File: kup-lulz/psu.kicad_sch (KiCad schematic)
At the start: 117 parts, among them J1 CONN_PCIE_PWR_8PIN, J2 CONN_IBC_MGMT, J3 CONN_01X03, J4 CONN_01X05, Q1 SSM6N58NU, SW1 SWITCH, SW2 SWITCH, U1 STM32L031C6U6, U2 MYMGK1R812ERSR, U3 MYMGK1R812ERSR, U4 MYMGK00506ERSR, U5 MYMGK00504ERSR, U6 MYMGK00504ERSR, U7 MYMGK00504ERSR, U8 ADP1740ACPZ-1.8-R7

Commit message: Continued initial work on kup-lulz devboard
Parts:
- C40, C41: footprint (none) -> azonenberg_pcb:EIA_0603_CAP_NOSILK
- Q1: footprint (none) -> azonenberg_pcb:DFN_6_0.65MM_2x2MM_GDS
- R31: footprint (none) -> azonenberg_pcb:EIA_0402_RES_NOSILK
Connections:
- net 1V8: no longer U4.5 (SENSE)
- net 3V3: now also U4.5 (SENSE)
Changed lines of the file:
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@@
   (title_block
     (title "Kintex Ultrascale+ OshPark For The Lulz")
-    (date "2024-01-31")
+    (date "2024-02-01")
     (rev "0.1")
   )
@@
     (effects (font (size 1.27 1.27)) (justify left bottom))
   )
-  (label "1V8" (at 245.11 109.22 0)
+  (label "3V3" (at 245.11 109.22 0)
     (effects (font (size 1.27 1.27)) (justify left bottom))
   )
@@
     (effects (font (size 1.27 1.27)) (justify right))
   )
-  (hierarchical_label "FPGA_INIT" (shape bidirectional) (at 91.44 393.7 180)
+  (hierarchical_label "FPGA_INIT" (shape input) (at 91.44 393.7 180)
     (effects (font (size 1.27 1.27)) (justify right))
   )
@@
       (effects (font (size 1.27 1.27)) (justify left))
     )
-    (property "Footprint" "" (id 2) (at 357.8352 154.94 0)
+    (property "Footprint" "azonenberg_pcb:EIA_0603_CAP_NOSILK" (id 2) (at 357.8352 154.94 0)
       (effects (font (size 1.27 1.27)) hide)
     )
@@
       (effects (font (size 1.524 1.524)) (justify left))
     )
-    (property "Footprint" "" (id 2) (at 382.27 204.47 0)
+    (property "Footprint" "azonenberg_pcb:DFN_6_0.65MM_2x2MM_GDS" (id 2) (at 382.27 204.47 0)
       (effects (font (size 1.524 1.524)) hide)
     )
@@
       (effects (font (size 1.27 1.27)) (justify left))
     )
-    (property "Footprint" "" (id 2) (at 406.0952 154.94 0)
+    (property "Footprint" "azonenberg_pcb:EIA_0603_CAP_NOSILK" (id 2) (at 406.0952 154.94 0)
       (effects (font (size 1.27 1.27)) hide)
     )
@@
       (effects (font (size 1.27 1.27)) (justify left))
     )
-    (property "Footprint" "" (id 2) (at 383.032 193.04 90)
+    (property "Footprint" "azonenberg_pcb:EIA_0402_RES_NOSILK" (id 2) (at 383.032 193.04 90)
       (effects (font (size 1.27 1.27)) hide)
     )

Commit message: Continued initial layout of kup-lulz
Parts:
- C39: footprint (none) -> azonenberg_pcb:EIA_0402_CAP_NOSILK
- U8: footprint (none) -> azonenberg_pcb:QFN_16_0.65MM_4x4MM
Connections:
- net GND: now also U8.6 (GND), U8.PAD (GND)
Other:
- company: (none) -> Antikernel Labs
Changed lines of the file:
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@@
   (title_block
     (title "Kintex Ultrascale+ OshPark For The Lulz")
-    (date "2024-02-01")
+    (date "2024-02-05")
     (rev "0.1")
+    (company "Antikernel Labs")
+    (comment 1 "Andrew D. Zonenberg")
   )
   (junction (at 222.25 139.7) (diameter 0) (color 0 0 0 0)
@@
     (effects (font (size 1.27 1.27)) (justify right bottom))
   )
+  (label "GND" (at 369.57 170.18 180)
+    (effects (font (size 1.27 1.27)) (justify right bottom))
+  )
   (label "BOOT0" (at 195.58 401.32 180)
     (effects (font (size 1.27 1.27)) (justify right bottom))
@@
     (property "Reference" "U8" (id 0) (at 384.175 142.4772 0))
     (property "Value" "ADP1740ACPZ-1.8-R7" (id 1) (at 384.175 145.0141 0))
-    (property "Footprint" "" (id 2) (at 374.65 175.26 0)
+    (property "Footprint" "azonenberg_pcb:QFN_16_0.65MM_4x4MM" (id 2) (at 374.65 175.26 0)
       (effects (font (size 1.27 1.27)) hide)
     )
@@
       (effects (font (size 1.27 1.27)) (justify left))
     )
-    (property "Footprint" "" (id 2) (at 348.9452 170.18 0)
+    (property "Footprint" "azonenberg_pcb:EIA_0402_CAP_NOSILK" (id 2) (at 348.9452 170.18 0)
       (effects (font (size 1.27 1.27)) hide)
     )

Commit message: Continued initial layout
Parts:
- removed C14, C18: 22 uF 25V, azonenberg_pcb:EIA_1812_CAP_NOSILK, symbol device:C
- removed C28, C32: 220 uF, azonenberg_pcb:EIA_1210_CAP_NOSILK, symbol device:C
- removed C36: DNP, azonenberg_pcb:EIA_1210_CAP_NOSILK, symbol device:C
- removed R18: 3k, azonenberg_pcb:EIA_0402_RES_NOSILK, symbol device:R
- removed R22: 160, azonenberg_pcb:EIA_0402_RES_NOSILK, symbol device:R
- removed R36: 10K, azonenberg_pcb:EIA_0402_RES_NOSILK, symbol device:R
- removed R37: 1K, azonenberg_pcb:EIA_0402_RES_NOSILK, symbol device:R
- removed TP17: U.FL, azonenberg_pcb:CONN_U.FL_TE_1909763-1, symbol conn:CONN_COAXIAL
- removed TP5: TESTPOINT, azonenberg_pcb:TESTPOINT_SMT_0.5MM, symbol conn:CONN_01X01
- removed U6: MYMGK00504ERSR, azonenberg_pcb:MODULE_MURATA_MYMGK00504ERSR, symbol power-azonenberg:MYMGK00504ERSR
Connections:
- net 2V5 is gone; now on net 3V3: C40.1, R31.1, U8.1 (VIN), U8.15 (VIN), U8.16 (VIN), U8.2 (VIN), U8.3 (VIN)
- net 2V5_EN: no longer names the net of U1.1 (PC0)
- net 2V5_PGOOD: no longer names the net of U1.2 (PC13)
- net GVEN_2V5 renamed GVEN_3V3
- no-connect marks 4 -> 6
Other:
- note added: "220 mA @ 1.8V regulated from some other rail Use 3V3 for input on test board to eliminate need for 2V5 rail on an already dense PCB"
- note added: "Level shift GTY_VCCAUX_EN to 3.3V levels since EN of ADP1740 should not exceed VIN"
- note removed: "220 mA @ 1.8V regulated from some other rail 2V5 has plenty of headroom if regulator has <700 mV dropout"
- note removed: "Level shift GTY_VCCAUX_EN to 2.5V levels since EN of ADP1740 should not exceed VIN"
- moved on the sheet: TP16

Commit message: Continued initial routing
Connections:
- net 1V8_EN: now also U1.4 (PC15); no longer U1.27 (PB14)
- net 1V8_PGOOD: now also U1.3 (PC14); no longer U1.28 (PB15)
- net 3V3_EN: now also U1.10 (PA0); no longer U1.20 (PB2)
- net 3V3_PGOOD: now also U1.11 (PA1); no longer U1.18 (PB0)
- net FPGA_RST_N: now also U1.18 (PB0); no longer U1.11 (PA1)
- net GTY_VCCAUX_EN_N: now also U1.28 (PB15); no longer U1.3 (PC14)
- net GTY_VCCAUX_PGOOD: now also U1.27 (PB14); no longer U1.4 (PC15)
- net GTY_VCC_EN: now also U1.12 (PA2); no longer U1.21 (PB10)
- net GTY_VTT_EN: now also U1.30 (PA9); no longer U1.41 (PB5)
- net MCU_READY: now also U1.20 (PB2); no longer U1.10 (PA0)
- net MCU_RST_N: now also U1.21 (PB10); no longer U1.12 (PA2)
- net SUPER_I2C_SCL: now also U1.45 (PB8); no longer U1.30 (PA9)
- net SUPER_I2C_SDA: now also U1.46 (PB9); no longer U1.31 (PA10)
- net VCCINT_EN: now also U1.2 (PC13); no longer U1.39 (PB3)
- net VCCINT_PGOOD: now also U1.1 (PC0); no longer U1.32 (PA11)
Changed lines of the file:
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@@
   )
   (no_connect (at 48.26 370.84))
-  (no_connect (at 130.81 396.24))
-  (no_connect (at 91.44 383.54))
-  (no_connect (at 91.44 386.08))
+  (no_connect (at 91.44 375.92))
+  (no_connect (at 48.26 391.16))
+  (no_connect (at 91.44 370.84))
   (no_connect (at 91.44 373.38))
-  (no_connect (at 130.81 393.7))
+  (no_connect (at 48.26 388.62))
   (wire (pts (xy 67.31 214.63) (xy 67.31 217.17))
     (stroke (width 0) (type default) (color 0 0 0 0))
@@
     (effects (font (size 1.27 1.27)) (justify right bottom))
   )
-  (label "1V8_PGOOD" (at 91.44 401.32 180)
+  (label "1V8_PGOOD" (at 130.81 398.78 180)
     (effects (font (size 1.27 1.27)) (justify right bottom))
   )
@@
     (effects (font (size 1.27 1.27)) (justify right bottom))
   )
-  (label "3V3_EN" (at 91.44 368.3 180)
+  (label "3V3_EN" (at 48.26 363.22 180)
     (effects (font (size 1.27 1.27)) (justify right bottom))
   )
@@
     (effects (font (size 1.27 1.27)) (justify left bottom))
   )
-  (label "SUPER_I2C_SDA" (at 48.26 388.62 180)
+  (label "SUPER_I2C_SDA" (at 91.44 386.08 180)
     (effects (font (size 1.27 1.27)) (justify right bottom))
   )
@@
     (effects (font (size 1.27 1.27)) (justify left bottom))
   )
-  (label "VCCINT_PGOOD" (at 48.26 391.16 180)
+  (label "VCCINT_PGOOD" (at 130.81 393.7 180)
     (effects (font (size 1.27 1.27)) (justify right bottom))
   )
@@
     (effects (font (size 1.27 1.27)) (justify right bottom))
   )
-  (label "GTY_VCCAUX_PGOOD" (at 130.81 401.32 180)
+  (label "GTY_VCCAUX_PGOOD" (at 91.44 398.78 180)
     (effects (font (size 1.27 1.27)) (justify right bottom))
   )
@@
     (effects (font (size 1.27 1.27)) (justify right bottom))
   )
-  (label "VCCINT_EN" (at 91.44 370.84 180)
+  (label "VCCINT_EN" (at 130.81 396.24 180)
     (effects (font (size 1.27 1.27)) (justify right bottom))
   )
@@
     (effects (font (size 1.27 1.27)) (justify right bottom))
   )
-  (label "1V8_EN" (at 91.44 398.78 180)
+  (label "1V8_EN" (at 130.81 401.32 180)
     (effects (font (size 1.27 1.27)) (justify right bottom))
   )
-  (label "GTY_VTT_EN" (at 91.44 375.92 180)
+  (label "GTY_VTT_EN" (at 48.26 386.08 180)
     (effects (font (size 1.27 1.27)) (justify right bottom))
   )
@@
     (effects (font (size 1.27 1.27)) (justify right bottom))
   )
-  (label "SUPER_I2C_SCL" (at 48.26 386.08 180)
+  (label "SUPER_I2C_SCL" (at 91.44 383.54 180)
     (effects (font (size 1.27 1.27)) (justify right bottom))
   )
@@
     (effects (font (size 1.27 1.27)) (justify left bottom))
   )
-  (label "3V3_PGOOD" (at 91.44 363.22 180)
+  (label "3V3_PGOOD" (at 48.26 365.76 180)
     (effects (font (size 1.27 1.27)) (justify right bottom))
   )
@@
     (effects (font (size 1.27 1.27)) (justify right bottom))
   )
-  (label "GTY_VCCAUX_EN_N" (at 130.81 398.78 180)
+  (label "GTY_VCCAUX_EN_N" (at 91.44 401.32 180)
     (effects (font (size 1.27 1.27)) (justify right bottom))
   )
@@
     (effects (font (size 1.27 1.27)) (justify right bottom))
   )
-  (label "GTY_VCC_EN" (at 91.44 388.62 180)
+  (label "GTY_VCC_EN" (at 48.26 368.3 180)
     (effects (font (size 1.27 1.27)) (justify right bottom))
   )
@@
     (effects (font (size 1.27 1.27)) (justify right))
   )
-  (hierarchical_label "MCU_READY" (shape input) (at 48.26 363.22 180)
+  (hierarchical_label "MCU_READY" (shape input) (at 91.44 368.3 180)
     (effects (font (size 1.27 1.27)) (justify right))
   )
@@
     (effects (font (size 1.27 1.27)) (justify left))
   )
-  (hierarchical_label "MCU_RST_N" (shape output) (at 48.26 368.3 180)
+  (hierarchical_label "MCU_RST_N" (shape output) (at 91.44 388.62 180)
     (effects (font (size 1.27 1.27)) (justify right))
   )
@@
     (effects (font (size 1.27 1.27)) (justify right))
   )
-  (hierarchical_label "FPGA_RST_N" (shape output) (at 48.26 365.76 180)
+  (hierarchical_label "FPGA_RST_N" (shape output) (at 91.44 363.22 180)
     (effects (font (size 1.27 1.27)) (justify right))
   )
@@
     (pin "17")
     (pin "29")
-    (pin "30" (alternate "I2C1_SCL"))
-    (pin "31" (alternate "I2C1_SDA"))
+    (pin "30")
+    (pin "31")
     (pin "32")
     (pin "33")
@@
     (pin "40")
     (pin "41")
-    (pin "42")
-    (pin "43")
-    (pin "45")
-    (pin "46")
+    (pin "42" (alternate "USART2_TX"))
+    (pin "43" (alternate "USART2_RX"))
+    (pin "45" (alternate "I2C1_SCL"))
+    (pin "46" (alternate "I2C1_SDA"))
     (pin "1")
     (pin "2")
@@
     (pin "17")
     (pin "29")
-    (pin "30" (alternate "I2C1_SCL"))
-    (pin "31" (alternate "I2C1_SDA"))
+    (pin "30")
+    (pin "31")
     (pin "32")
     (pin "33")
@@
     (pin "40")
     (pin "41")
-    (pin "42")
-    (pin "43")
-    (pin "45")
-    (pin "46")
+    (pin "42" (alternate "USART2_TX"))
+    (pin "43" (alternate "USART2_RX"))
+    (pin "45" (alternate "I2C1_SCL"))
+    (pin "46" (alternate "I2C1_SDA"))
     (pin "1")
     (pin "2")
@@
     (pin "15" (alternate "SPI1_SCK"))
     (pin "16" (alternate "SPI1_MISO"))
-    (pin "17" (alternate "SPI1_MOSI"))
+    (pin "17")
     (pin "29")
-    (pin "30" (alternate "I2C1_SCL"))
-    (pin "31" (alternate "I2C1_SDA"))
+    (pin "30")
+    (pin "31")
     (pin "32")
     (pin "33")
-    (pin "34" (alternate "SWDIO"))
-    (pin "37" (alternate "SWCLK"))
+    (pin "34")
+    (pin "37")
     (pin "38")
     (pin "18")
@@
     (pin "40")
     (pin "41")
-    (pin "42")
-    (pin "43")
-    (pin "45")
-    (pin "46")
+    (pin "42" (alternate "USART2_TX"))
+    (pin "43" (alternate "USART2_RX"))
+    (pin "45" (alternate "I2C1_SCL"))
+    (pin "46" (alternate "I2C1_SDA"))
     (pin "1")
     (pin "2")
@@
     (pin "17")
     (pin "29")
-    (pin "30" (alternate "I2C1_SCL"))
-    (pin "31" (alternate "I2C1_SDA"))
+    (pin "30")
+    (pin "31")
     (pin "32")
     (pin "33")
@@
     (pin "40")
     (pin "41")
-    (pin "42")
-    (pin "43")
-    (pin "45")
-    (pin "46")
+    (pin "42" (alternate "USART2_TX"))
+    (pin "43" (alternate "USART2_RX"))
+    (pin "45" (alternate "I2C1_SCL"))
+    (pin "46" (alternate "I2C1_SDA"))
     (pin "1")
     (pin "2")
@@
     (pin "17")
     (pin "29")
-    (pin "30" (alternate "I2C1_SCL"))
-    (pin "31" (alternate "I2C1_SDA"))
+    (pin "30")
+    (pin "31")
     (pin "32")
     (pin "33")
@@
     (pin "42" (alternate "USART2_TX"))
     (pin "43" (alternate "USART2_RX"))
-    (pin "45")
-    (pin "46")
+    (pin "45" (alternate "I2C1_SCL"))
+    (pin "46" (alternate "I2C1_SDA"))
     (pin "1")
     (pin "2")

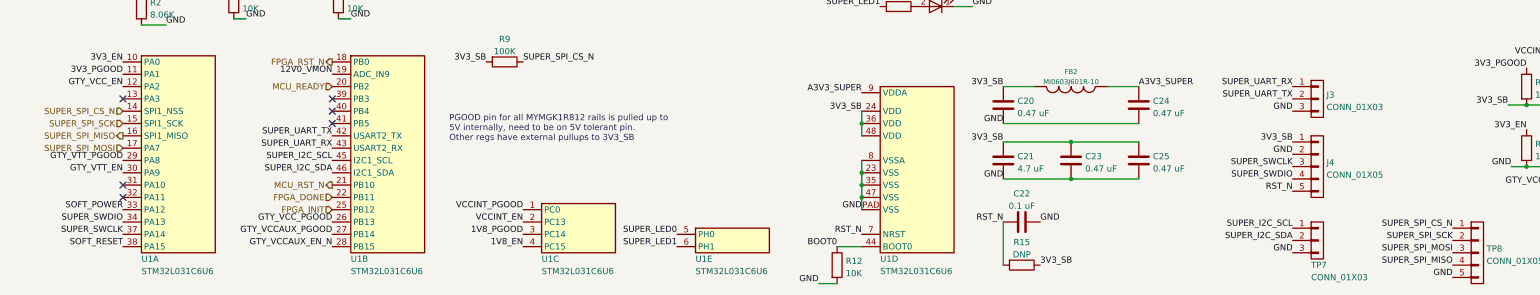
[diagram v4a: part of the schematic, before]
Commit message: Continued kup-lulz routing. Deleted one of the PMODs as there's no way it will fit.
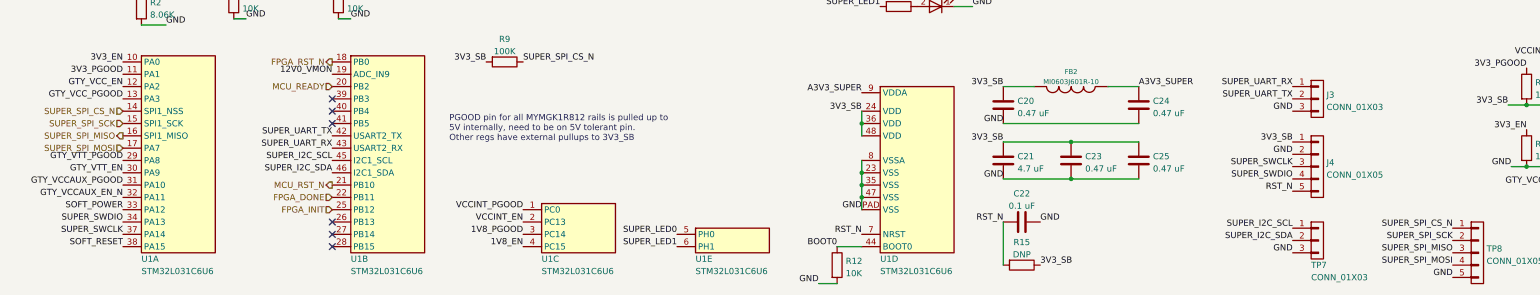
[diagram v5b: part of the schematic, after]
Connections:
- net GTY_VCCAUX_EN_N: now also U1.32 (PA11); no longer U1.28 (PB15)
- net GTY_VCCAUX_PGOOD: now also U1.31 (PA10); no longer U1.27 (PB14)
- net GTY_VCC_PGOOD: now also U1.13 (PA3); no longer U1.26 (PB13)
- net SUPER_SPI_MISO: now also TP8.3 (P3); no longer TP8.4 (P4)
- net SUPER_SPI_MOSI: now also TP8.4 (P4); no longer TP8.3 (P3)
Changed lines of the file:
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@@
   (title_block
     (title "Kintex Ultrascale+ OshPark For The Lulz")
-    (date "2024-02-05")
+    (date "2024-02-06")
     (rev "0.1")
     (company "Antikernel Labs")
@@
   (junction (at 222.25 142.24) (diameter 0) (color 0 0 0 0)
   )
-  (no_connect (at 48.26 370.84))
   (no_connect (at 91.44 375.92))
-  (no_connect (at 48.26 391.16))
+  (no_connect (at 91.44 398.78))
+  (no_connect (at 91.44 396.24))
+  (no_connect (at 91.44 401.32))
   (no_connect (at 91.44 370.84))
   (no_connect (at 91.44 373.38))
-  (no_connect (at 48.26 388.62))
   (wire (pts (xy 67.31 214.63) (xy 67.31 217.17))
     (stroke (width 0) (type default) (color 0 0 0 0))
@@
     (effects (font (size 1.27 1.27)) (justify left bottom))
   )
-  (label "GTY_VCC_PGOOD" (at 91.44 396.24 180)
+  (label "GTY_VCC_PGOOD" (at 48.26 370.84 180)
     (effects (font (size 1.27 1.27)) (justify right bottom))
   )
@@
     (effects (font (size 1.27 1.27)) (justify right bottom))
   )
-  (label "GTY_VCCAUX_PGOOD" (at 91.44 398.78 180)
+  (label "GTY_VCCAUX_PGOOD" (at 48.26 388.62 180)
     (effects (font (size 1.27 1.27)) (justify right bottom))
   )
@@
     (effects (font (size 1.27 1.27)) (justify right bottom))
   )
-  (label "SUPER_SPI_MOSI" (at 322.58 402.59 180)
+  (label "SUPER_SPI_MOSI" (at 322.58 405.13 180)
     (effects (font (size 1.27 1.27)) (justify right bottom))
   )
@@
     (effects (font (size 1.27 1.27)) (justify right bottom))
   )
-  (label "SUPER_SPI_MISO" (at 322.58 405.13 180)
+  (label "SUPER_SPI_MISO" (at 322.58 402.59 180)
     (effects (font (size 1.27 1.27)) (justify right bottom))
   )
@@
     (effects (font (size 1.27 1.27)) (justify right bottom))
   )
-  (label "GTY_VCCAUX_EN_N" (at 91.44 401.32 180)
-    (effects (font (size 1.27 1.27)) (justify right bottom))
-  )
+  (label "GTY_VCCAUX_EN_N" (at 48.26 391.16 180)
+    (effects (font (size 1.27 1.27)) (justify right bottom))
+  )

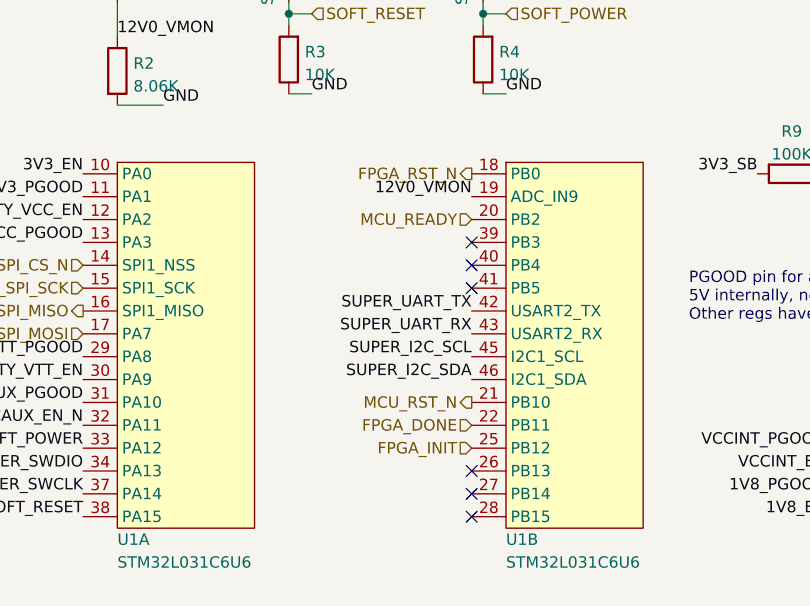
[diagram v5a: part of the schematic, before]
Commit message: FPGA is fully scaped, maybe? just need to hook up MCU now
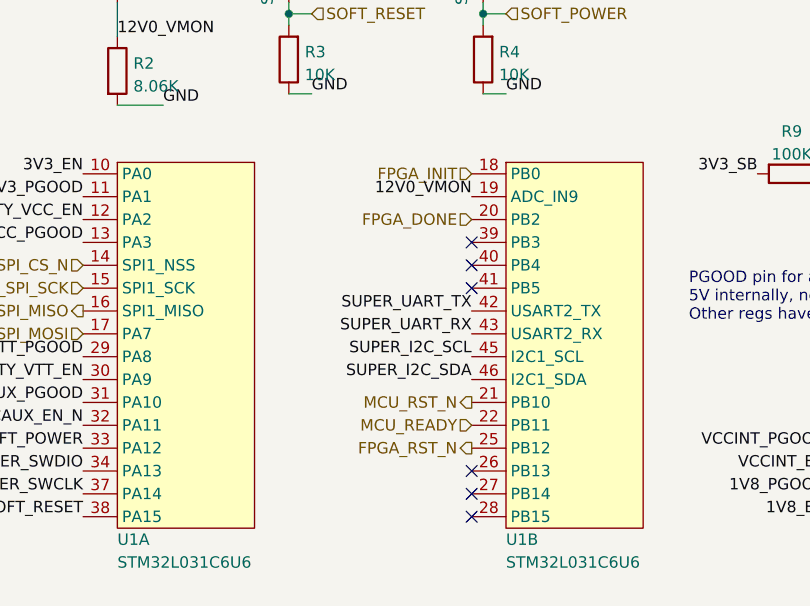
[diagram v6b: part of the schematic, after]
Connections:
- net FPGA_DONE: now also U1.20 (PB2); no longer U1.22 (PB11)
- net FPGA_INIT: now also U1.18 (PB0); no longer U1.25 (PB12)
- net FPGA_RST_N: now also U1.25 (PB12); no longer U1.18 (PB0)
- net MCU_READY: now also U1.22 (PB11); no longer U1.20 (PB2)
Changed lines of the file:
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@@
   (title_block
     (title "Kintex Ultrascale+ OshPark For The Lulz")
-    (date "2024-02-06")
+    (date "2024-02-08")
     (rev "0.1")
     (company "Antikernel Labs")
@@
     (effects (font (size 1.27 1.27)) (justify left))
   )
-  (hierarchical_label "FPGA_DONE" (shape input) (at 91.44 391.16 180)
+  (hierarchical_label "FPGA_DONE" (shape input) (at 91.44 368.3 180)
     (effects (font (size 1.27 1.27)) (justify right))
   )
@@
     (effects (font (size 1.27 1.27)) (justify right))
   )
-  (hierarchical_label "MCU_READY" (shape input) (at 91.44 368.3 180)
+  (hierarchical_label "MCU_READY" (shape input) (at 91.44 391.16 180)
     (effects (font (size 1.27 1.27)) (justify right))
   )
@@
     (effects (font (size 1.27 1.27)) (justify right))
   )
-  (hierarchical_label "FPGA_INIT" (shape input) (at 91.44 393.7 180)
+  (hierarchical_label "FPGA_INIT" (shape input) (at 91.44 363.22 180)
     (effects (font (size 1.27 1.27)) (justify right))
   )
-  (hierarchical_label "FPGA_RST_N" (shape output) (at 91.44 363.22 180)
+  (hierarchical_label "FPGA_RST_N" (shape output) (at 91.44 393.7 180)
     (effects (font (size 1.27 1.27)) (justify right))
   )
